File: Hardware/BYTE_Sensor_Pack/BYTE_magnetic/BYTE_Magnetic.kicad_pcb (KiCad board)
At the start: 2 copper layers, 18 x 23 mm, 16 parts, among them J1 PCB, U1 SI7210-B-11-IM2, U2 DRV2605YZFR, U4 SI7210-B-12-IM2, U5 SI7210-B-13-IM2, U6 SI7210-B-14-IM2

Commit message: update magnetic layout
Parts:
- removed C1, C2: 0.1uF, Capacitor_SMD:C_0603_1608Metric
- removed the J1 at (146.4, 110.9)
- removed R3: 2.2K, Resistor_SMD:R_0603_1608Metric
- removed U2: DRV2605YZFR, BYTE_Sensors:BGA9C50P3X3_144X144X62
- added J1: Input, BYTE_Sensors:Flex_Connector, F.Cu at (181.9, 121.9)
- added J1: PCB, BYTE_Sensors:Senor_Only_PCB, F.Cu at (182.9, 114.9)
- added Ref**: Val**, BYTE_Sensors:Logo, F.Cu at (177.7, 92.4)
- C4, C5, R1, R2: moved to B.Cu
- U1: value SI7210-B-11-IM2 -> DRV2605LDGS; footprint BYTE_Sensors:SON40P140X160X40-8N-D -> Package_SO:VSSOP-10_3x3mm_P0.5mm; moved to B.Cu
- moved U1 49.4 mm to (187.6, 118.8), turned to 90 degrees
- moved R1 45.8 mm to (183.7, 117.1), turned to 270 degrees
- moved C4 44.5 mm to (190.1, 117.2), turned to 90 degrees
- moved R2 44.2 mm to (182.2, 117.1), turned to 270 degrees
- moved U6 40.9 mm to (186.3, 115.5), turned to 45 degrees
- moved C7 39.7 mm to (185.1, 114.2), turned to 225 degrees
- moved C3 37.8 mm to (179.1, 114.2), turned to 135 degrees
- moved U5 36.8 mm to (182.0, 106.6)
- moved C6 36.7 mm to (182.0, 108.5)
- moved C5 35.5 mm to (185.1, 117.1)
- moved U4 27.6 mm to (177.9, 115.5), turned to 315 degrees
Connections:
- C4 pad 1: /REG -> Net-(C4-Pad1)
- U1 pad 1: GND -> Net-(C4-Pad1)
- U1 pad 3: Net-(U1-Pad3) -> /SDA
- U1 pad 4: /SDA -> /IN_TRIG
- U1 pad 5: GND -> /EN
- U1 pad 6: Net-(U1-Pad6) -> +3V3
- U1 pad 7: Net-(U1-Pad3) -> Net-(M1-Pad1)
- U1 pad 8: +3V3 -> GND
- U4 pad 3: Net-(U4-Pad3) -> (no net)
- U4 pad 7: Net-(U4-Pad3) -> Net-(U4-Pad7)
- U5 pad 3: Net-(U5-Pad3) -> (no net)
- U5 pad 7: Net-(U5-Pad3) -> Net-(U5-Pad7)
- U6 pad 3: Net-(U6-Pad3) -> (no net)
- U6 pad 7: Net-(U6-Pad3) -> Net-(U6-Pad7)
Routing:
- net +3V3: track 0.00 -> 46.3 mm, vias 0 -> 1
- net /SCL: track 0.00 -> 43.7 mm, vias 0 -> 1
- net /SDA: track 0.00 -> 42.5 mm, vias 0 -> 2
- net GND: track 0.00 -> 20.6 mm, vias 0 -> 14
- net /IN_TRIG: track 0.00 -> 11.1 mm, vias 0 -> 1
- net Net-(C4-Pad1): track 0.00 -> 4.23 mm
- added copper zone on B.Cu, net GND
- added copper zone on F.Cu, net GND
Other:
- board text added: "3.3v"
- board text added: "GND"
- board text added: "INT"
- board text added: "SCL"
- board text added: "SDA"

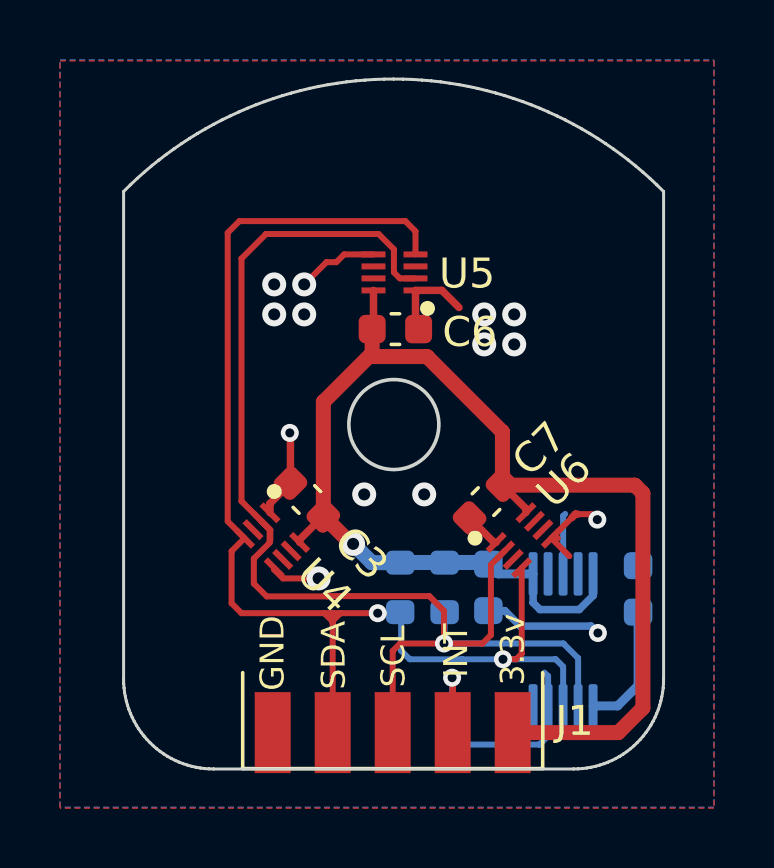
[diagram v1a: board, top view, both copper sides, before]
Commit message: modify magnetic
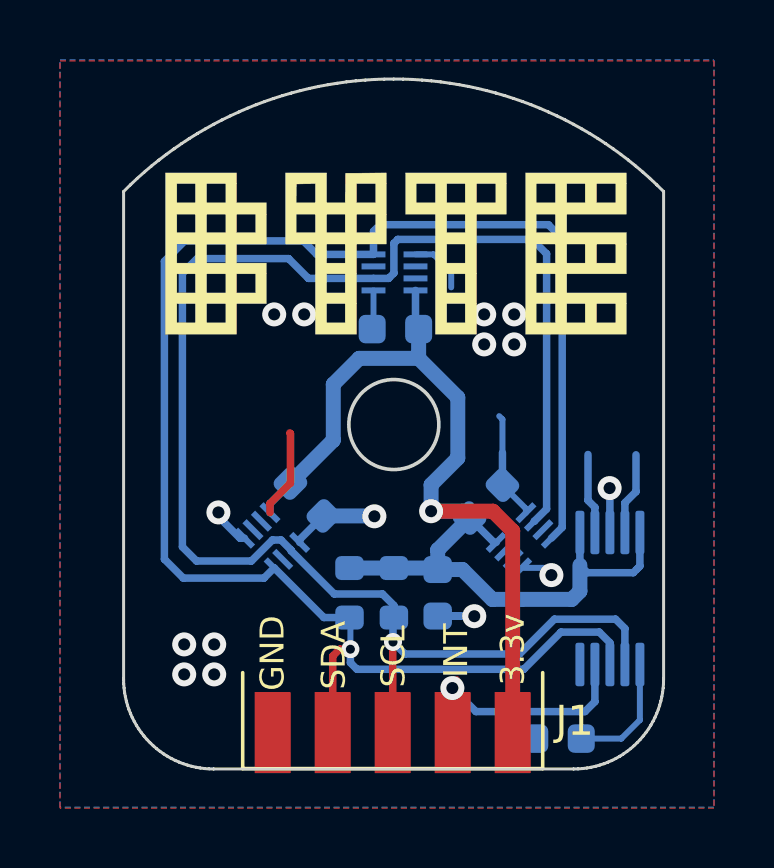
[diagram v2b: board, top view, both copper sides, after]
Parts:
- added Ref**: Val**, BYTE_Sensors:Logo, B.Cu at (186.4, 92.5)
- C3, C6, C7, U4, U5, U6: moved to B.Cu
- moved C4 5.66 mm to (187.5, 122.1), turned to 180 degrees
- moved U1 2.08 mm to (189.2, 117.5)
- moved C5 1.70 mm to (183.4, 117.3)
- moved R1 1.70 mm to (182.0, 117.3)
- moved R2 1.70 mm to (180.5, 117.3)
- turned C3 to 315 degrees
- turned C6 to 180 degrees
- turned C7 to 45 degrees
- turned U4 to 135 degrees
- turned U5 to 0 degrees
- turned U6 to 225 degrees
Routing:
- net /SDA: track 42.5 -> 57.2 mm, vias 2 -> 1
- net /SCL: track 43.7 -> 54.6 mm
- net Net-(M1-Pad2): track 0.00 -> 2.74 mm
- net Net-(M1-Pad1): track 0.00 -> 2.70 mm
- net +3V3: track 46.3 -> 44.6 mm
- net /IN_TRIG: track 11.1 -> 9.78 mm
- net GND: track 20.6 -> 20.0 mm, vias 14 -> 15

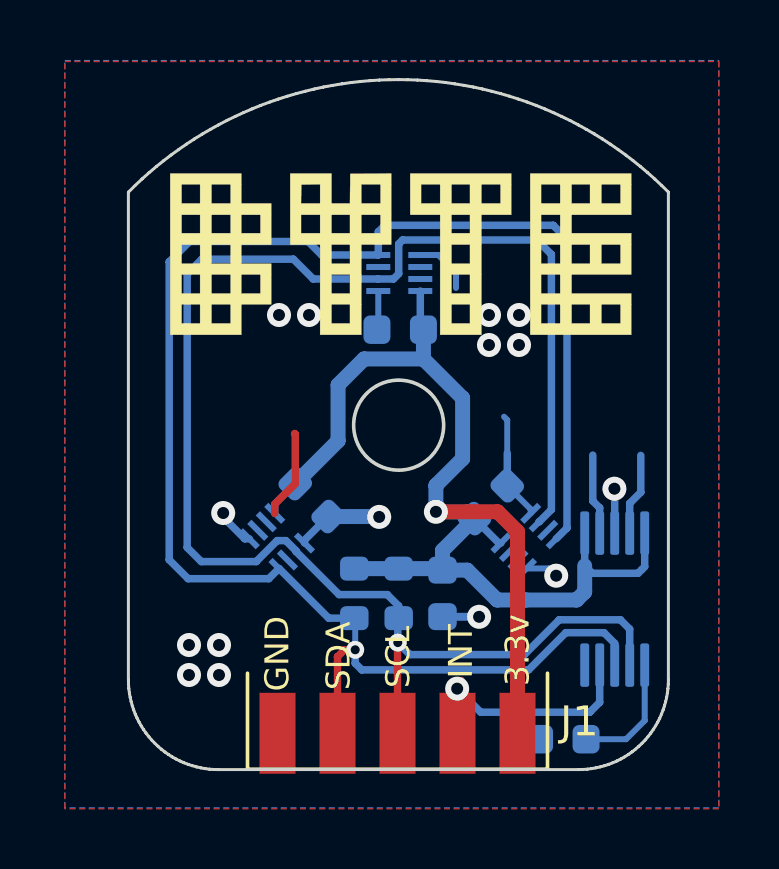
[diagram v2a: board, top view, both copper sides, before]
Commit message: update magnetic sensor, merge with FSR
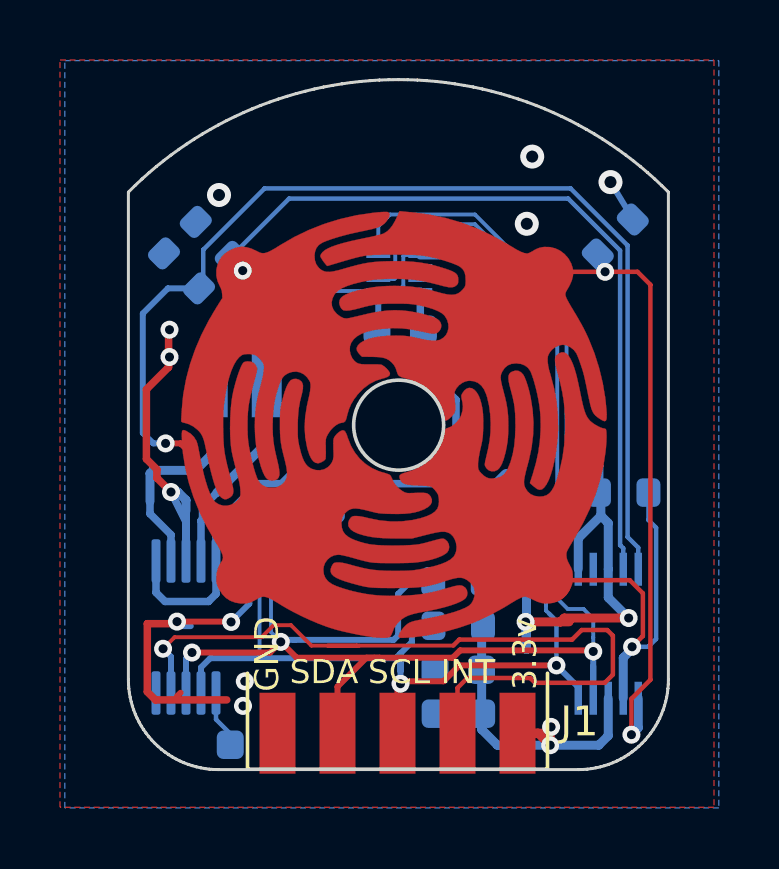
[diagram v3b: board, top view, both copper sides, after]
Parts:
- removed the Ref** at (186.4, 92.5)
- added C1: 1uF, Capacitor_SMD:C_0603_1608Metric, B.Cu at (184.0, 121.3)
- added J2: FSR, BYTE_Sensors:FSR_13mm, F.Cu at (182.0, 115.1)
- added M1: Motor_DC, BYTE_Sensors:VLV041235L, B.Cu at (177.7, 111.4)
- added R3: 10K, Resistor_SMD:R_0603_1608Metric, B.Cu at (189.5, 113.9)
- added R4: 10K, Resistor_SMD:R_0603_1608Metric, B.Cu at (189.2, 105.4)
- added R5: 10K, Resistor_SMD:R_0603_1608Metric, B.Cu at (174.8, 106.5)
- added R6: 10K, Resistor_SMD:R_0603_1608Metric, B.Cu at (175.8, 105.5)
- added U2: ADS1115IDGS, Package_SO:TSSOP-10_3x3mm_P0.5mm, B.Cu at (189.0, 118.6)
- moved U1 14.3 mm to (174.9, 118.4)
- moved C4 10.3 mm to (177.2, 122.3), turned to 0 degrees
- moved R2 3.48 mm to (184.0, 116.9), turned to 180 degrees
- moved C5 2.60 mm to (184.0, 119.8), turned to 180 degrees
- moved R1 2.26 mm to (184.0, 118.4), turned to 180 degrees
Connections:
- U4 pad 3: (no net) -> Net-(U4-Pad3)
- U4 pad 7: Net-(U4-Pad7) -> (no net)
- U5 pad 3: (no net) -> Net-(U5-Pad3)
- U5 pad 7: Net-(U5-Pad7) -> (no net)
- U6 pad 3: (no net) -> Net-(U6-Pad3)
- U6 pad 7: Net-(U6-Pad7) -> (no net)
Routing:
- net /A1: track 0.00 -> 41.0 mm, vias 0 -> 1
- net GND: track 20.0 -> 55.0 mm, vias 15 -> 13
- net /A0: track 0.00 -> 25.9 mm, vias 0 -> 1
- net /A2: track 0.00 -> 20.9 mm, vias 0 -> 2
- net /IN_TRIG: track 9.78 -> 26.9 mm
- net /A3: track 0.00 -> 13.0 mm, vias 0 -> 1
- net /SCL: track 54.6 -> 45.8 mm, vias 1 -> 2
- net Net-(M1-Pad1): track 2.70 -> 7.88 mm
- net +3V3: track 44.6 -> 40.4 mm, vias 1 -> 2
- net Net-(M1-Pad2): track 2.74 -> 6.80 mm
- net /SDA: track 57.2 -> 54.7 mm, vias 1 -> 3
- net Net-(C4-Pad1): track 4.06 -> 1.92 mm

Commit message: update pcbs
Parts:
- removed J2: FSR, BYTE_Sensors:FSR_13mm
- removed R1, R2: 2.2K, Resistor_SMD:R_0603_1608Metric
- removed R3, R4, R5, R6: 10K, Resistor_SMD:R_0603_1608Metric
- added REF**: Value, BYTE_Sensors:FSR_36, F.Cu at (182.0, 111.7)
- added RN1: R_Pack04, Resistor_SMD:R_Array_Convex_4x0603, B.Cu at (182.0, 116.8)
- moved C5 11.1 mm to (174.6, 113.9), turned to 0 degrees
- moved C1 8.97 mm to (188.9, 113.8), turned to 0 degrees
- moved C4 1.90 mm to (177.9, 120.6)
- moved U2 0.10 mm to (188.9, 118.6), turned to 90 degrees
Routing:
- net GND: track 55.0 -> 7.63 mm, vias 13 -> 8
- net /A1: track 41.0 -> 9.29 mm
- net /SDA: track 54.7 -> 24.9 mm, vias 3 -> 4
- net /SCL: track 45.8 -> 24.2 mm, vias 2 -> 4
- net /A0: track 25.9 -> 8.92 mm
- net /IN_TRIG: track 26.9 -> 12.9 mm
- net /A2: track 20.9 -> 8.44 mm, vias 2 -> 1
- net +3V3: track 40.4 -> 30.0 mm, vias 2 -> 5
- net /A3: track 13.0 -> 9.67 mm
- net Net-(M1-Pad1): track 7.88 -> 6.47 mm
- net Net-(C4-Pad1): track 1.92 -> 1.26 mm

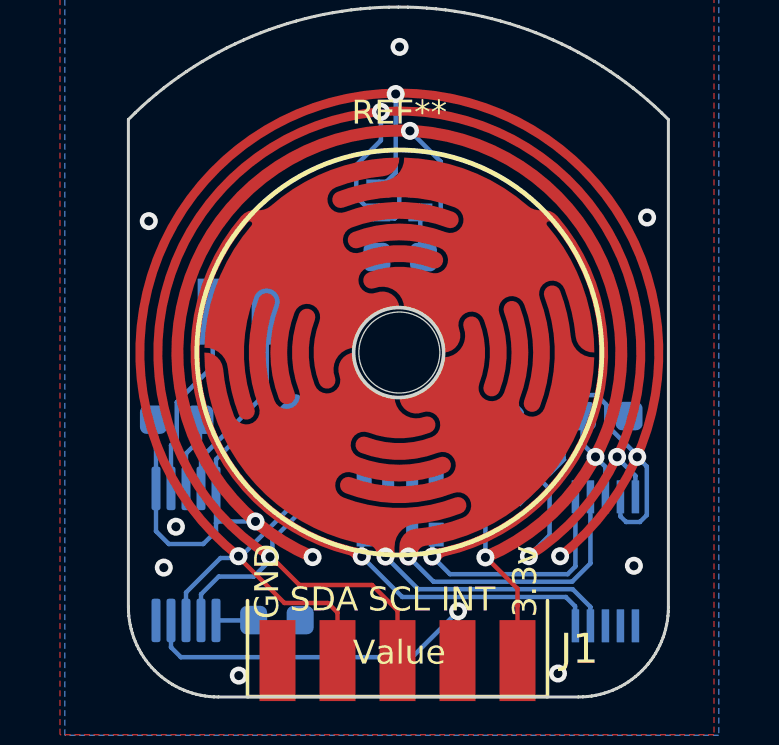
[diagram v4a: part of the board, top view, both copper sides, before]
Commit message: update gnd route
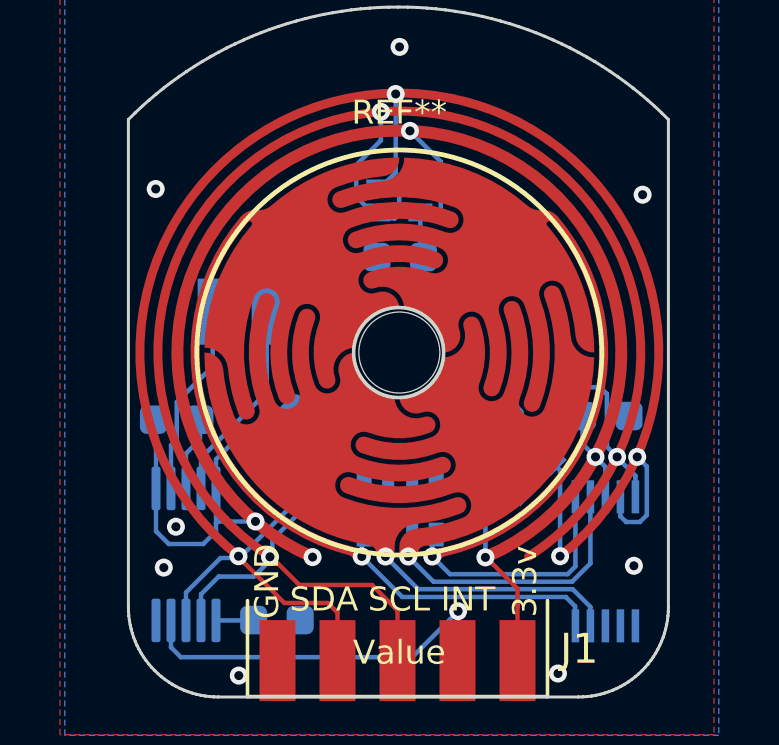
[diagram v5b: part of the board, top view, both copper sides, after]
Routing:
- net /SDA: track 24.9 -> 21.9 mm
- net GND: track 7.63 -> 9.88 mm
- net /SCL: track 24.2 -> 25.9 mm, vias 4 -> 3

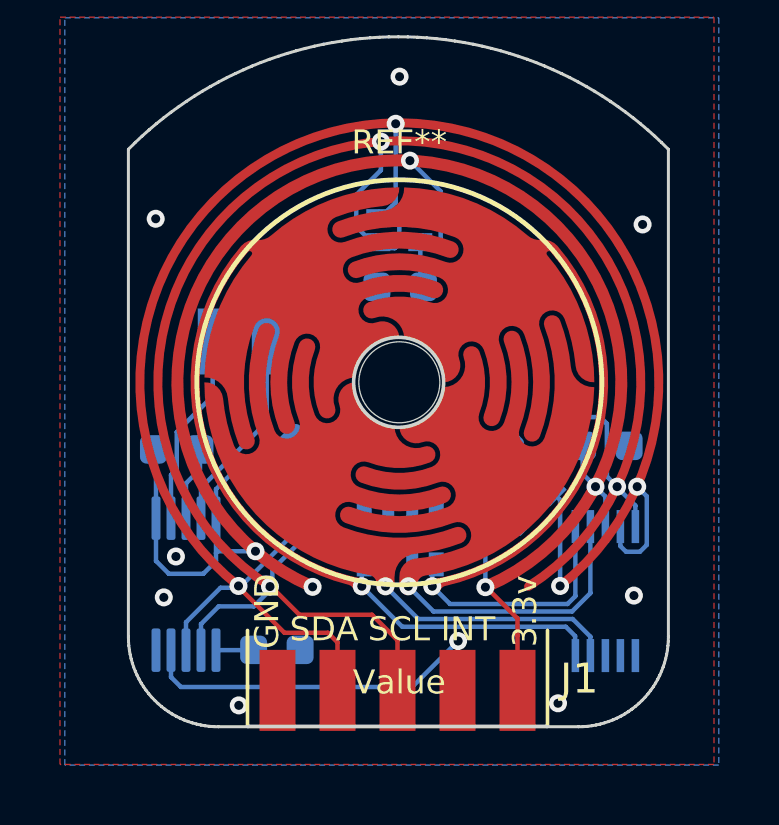
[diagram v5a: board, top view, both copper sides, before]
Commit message: update magentic adding I2C I/O controller
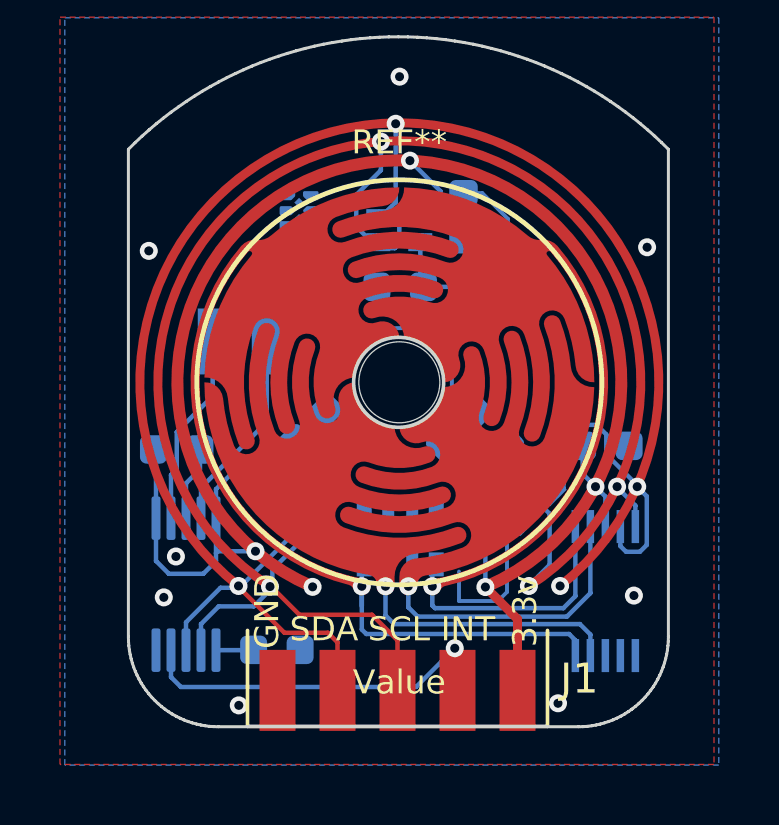
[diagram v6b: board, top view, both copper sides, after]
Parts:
- added D1: D_Small, Diode_SMD:D_0603_1608Metric, B.Cu at (180.1, 113.2)
- added D2: D_Small, Diode_SMD:D_0603_1608Metric, B.Cu at (184.2, 106.2)
- added D3: D_Small, Diode_SMD:D_0603_1608Metric, B.Cu at (184.0, 113.2)
- added U3: PTCA9416DTMR, BYTE_Sensors:PTCA9416DTMR, B.Cu at (178.7, 106.0)
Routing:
- net /magneticSignal: track 0.00 -> 18.0 mm
- net +3V3: track 30.0 -> 38.2 mm
- net Net-(D1-Pad2): track 0.00 -> 4.72 mm
- net Net-(D3-Pad2): track 0.00 -> 3.92 mm
- net /SDA: track 21.9 -> 24.9 mm
- net GND: track 9.88 -> 12.8 mm
- net /SCL: track 25.9 -> 24.1 mm, vias 3 -> 4
- net Net-(D2-Pad2): track 0.00 -> 1.66 mm
- net /A1: track 9.29 -> 10.6 mm
- net /A3: track 9.67 -> 10.7 mm
- net /A0: track 8.92 -> 9.53 mm

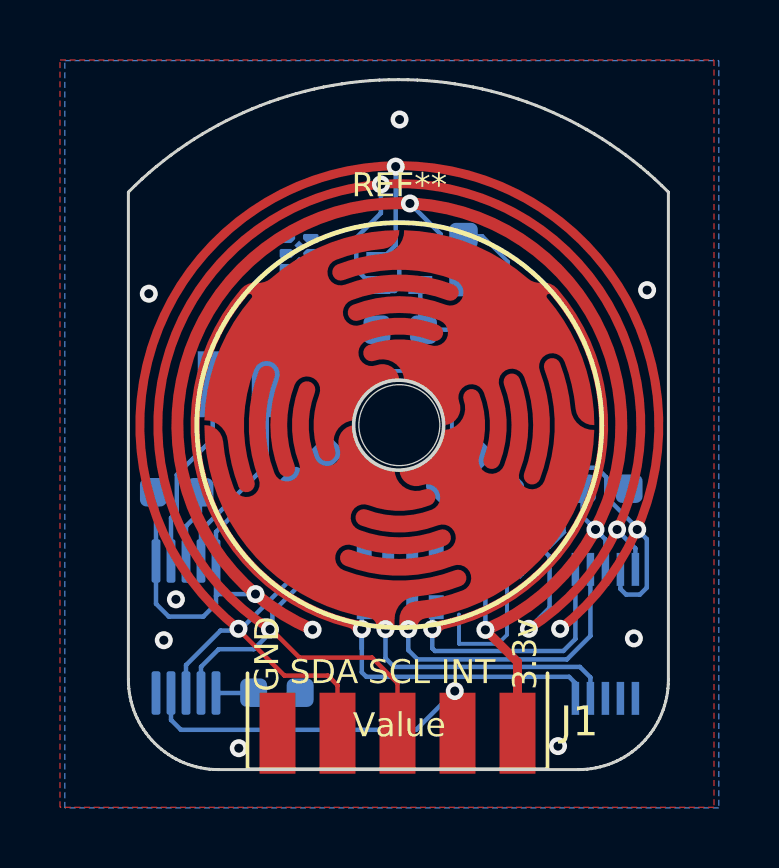
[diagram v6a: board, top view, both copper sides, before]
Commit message: update magnetic sensor
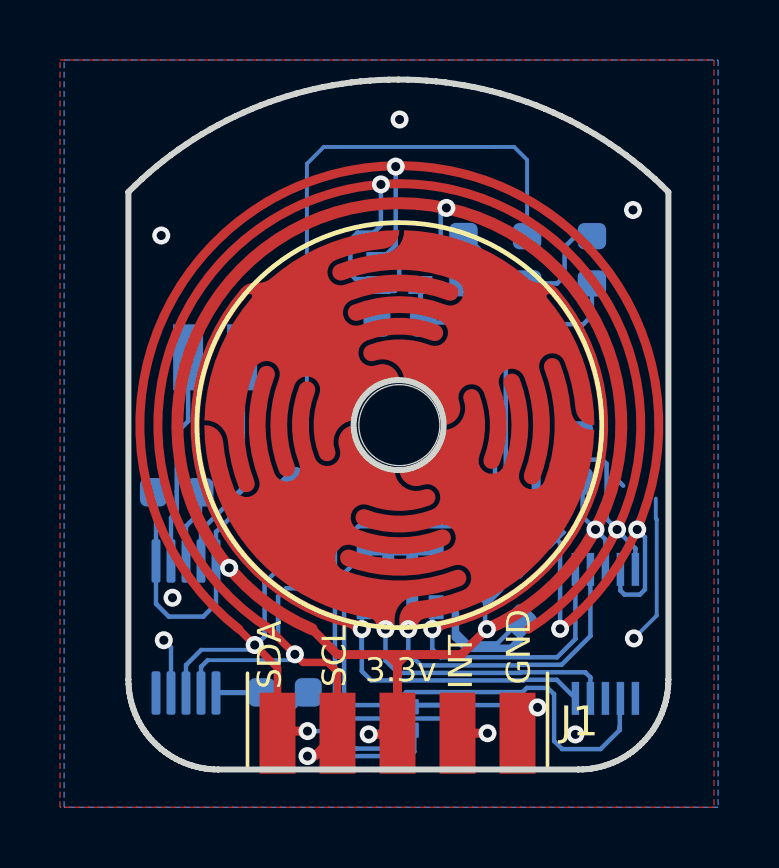
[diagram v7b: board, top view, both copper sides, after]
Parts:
- removed the J1 at (182.9, 114.9)
- U3: value PTCA9416DTMR -> PTCA9536BDTMR
- moved U3 15.9 mm to (182.0, 121.5), turned to 270 degrees
- moved D1 9.31 mm to (186.3, 106.2), turned to 90 degrees
- moved D3 8.30 mm to (188.4, 106.2), turned to 270 degrees
- moved C7 3.43 mm to (185.5, 117.6), turned to 315 degrees
- moved C1 1.37 mm to (188.0, 112.8), turned to 90 degrees
- moved M1 1.22 mm to (176.9, 110.5)
- moved C4 0.27 mm to (178.2, 120.6)
- moved C6 0.24 mm to (182.0, 108.2)
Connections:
- J1 pad 1: GND -> /SDA
- J1 pad 2: /SDA -> /SCL
- J1 pad 3: /SCL -> +3V3
- J1 pad 4: /IN_TRIG -> /INT_OUT
- J1 pad 5: +3V3 -> GND
- RN1 pad 5: GND -> /FSR_CTRL
- RN1 pad 6: GND -> /FSR_CTRL
- RN1 pad 7: GND -> /FSR_CTRL
- RN1 pad 8: GND -> /FSR_CTRL
- U1 pad 4: /IN_TRIG -> GND
- U2 pad 2: Net-(U2-Pad2) -> /ALERT
- U3 pad 1: Net-(U3-Pad1) -> /FSR_CTRL
- U3 pad 2: Net-(U3-Pad2) -> /ALERT
- U3 pad 3: Net-(U3-Pad3) -> GND
- U3 pad 4: Net-(U3-Pad4) -> /INT_OUT
- U3 pad 5: Net-(U3-Pad5) -> /SCL
- U3 pad 6: Net-(U3-Pad6) -> /SDA
- U3 pad 7: Net-(U3-Pad7) -> +3V3
- U3 pad 8: Net-(U3-Pad8) -> /magneticSignal
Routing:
- net GND: track 12.8 -> 32.9 mm
- net Net-(D1-Pad2): track 4.72 -> 24.5 mm
- net /IN_TRIG: track 12.5 -> 0.00 mm, vias 1 -> 0
- net /ALERT: track 0.00 -> 10.9 mm
- net /magneticSignal: track 18.0 -> 27.8 mm
- net /FSR_CTRL: track 0.00 -> 8.94 mm
- net Net-(D3-Pad2): track 3.92 -> 12.2 mm
- net /SCL: track 24.1 -> 32.3 mm
- net /INT_OUT: track 0.00 -> 3.87 mm, vias 0 -> 1
- net Net-(C4-Pad1): track 1.26 -> 2.79 mm
- net +3V3: track 38.2 -> 39.4 mm
- net Net-(M1-Pad1): track 6.47 -> 7.03 mm
- net Net-(M1-Pad2): track 6.80 -> 7.36 mm
- net /SDA: track 24.9 -> 25.4 mm, vias 4 -> 5

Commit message: update magnetic pcb and
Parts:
- moved M1 1.51 mm to (176.9, 112.0)
- moved C5 0.19 mm to (174.6, 114.1)
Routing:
- net GND: track 32.9 -> 37.7 mm
- net +3V3: track 39.4 -> 42.3 mm
- net /SDA: track 25.4 -> 28.2 mm
- net /A3: track 10.9 -> 13.0 mm
- net /A0: track 9.60 -> 11.2 mm
- net /A1: track 10.3 -> 11.9 mm
- net Net-(M1-Pad2): track 7.36 -> 5.83 mm
- net /SCL: track 32.3 -> 31.5 mm
- net /FSR_CTRL: track 8.94 -> 9.46 mm
